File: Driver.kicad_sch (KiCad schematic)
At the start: 20 parts, among them Q1 NMOS, Q2 NMOS, Q3 NMOS, Q4 NMOS

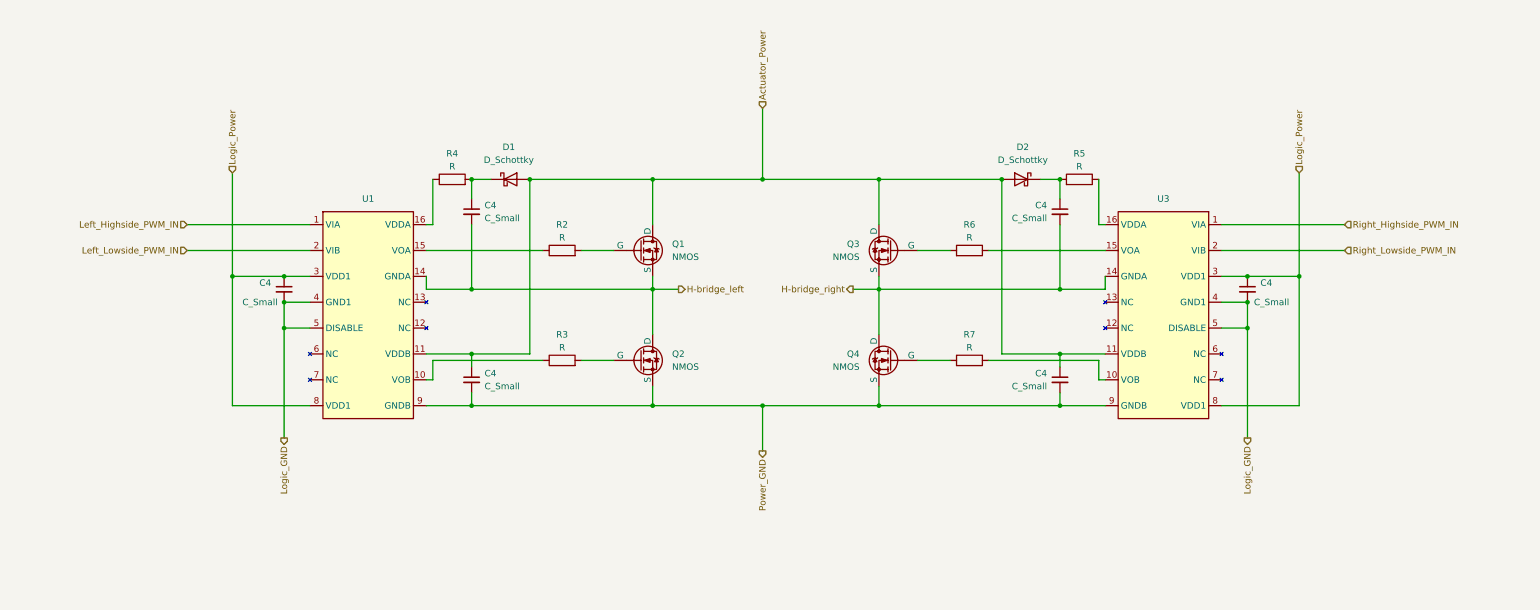
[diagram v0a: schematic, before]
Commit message: update Driver circuit
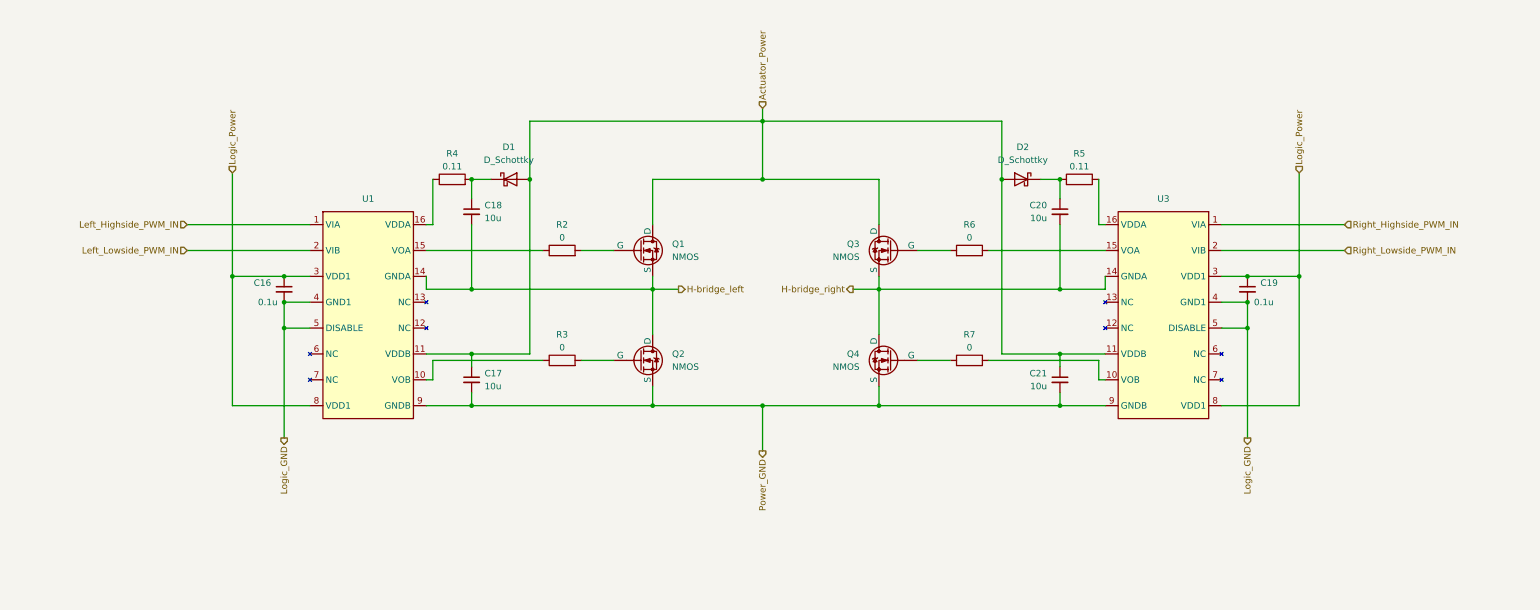
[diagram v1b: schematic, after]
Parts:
- C16, C19: renamed from C4; value C_Small -> 0.1u
- C17, C18, C20, C21: renamed from C4; value C_Small -> 10u
- R2, R3, R6, R7: value R -> 0
- R4, R5: value R -> 0.11
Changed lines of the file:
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@@
   (junction (at 127 106.68) (diameter 0) (color 0 0 0 0)
   )
+  (junction (at 54.61 109.22) (diameter 0) (color 0 0 0 0)
+  )
+  (junction (at 127 129.54) (diameter 0) (color 0 0 0 0)
+  )
+  (junction (at 148.59 73.66) (diameter 0) (color 0 0 0 0)
+  )
+  (junction (at 148.59 85.09) (diameter 0) (color 0 0 0 0)
+  )
+  (junction (at 243.84 104.14) (diameter 0) (color 0 0 0 0)
+  )
   (junction (at 195.58 85.09) (diameter 0) (color 0 0 0 0)
   )
-  (junction (at 54.61 109.22) (diameter 0) (color 0 0 0 0)
-  )
-  (junction (at 127 129.54) (diameter 0) (color 0 0 0 0)
-  )
-  (junction (at 171.45 85.09) (diameter 0) (color 0 0 0 0)
-  )
-  (junction (at 148.59 85.09) (diameter 0) (color 0 0 0 0)
-  )
-  (junction (at 243.84 104.14) (diameter 0) (color 0 0 0 0)
-  )
   (junction (at 243.84 114.3) (diameter 0) (color 0 0 0 0)
   )
@@
   (junction (at 44.45 104.14) (diameter 0) (color 0 0 0 0)
   )
+  (junction (at 102.87 85.09) (diameter 0) (color 0 0 0 0)
+  )
   (junction (at 207.01 129.54) (diameter 0) (color 0 0 0 0)
   )
@@
   (junction (at 243.84 109.22) (diameter 0) (color 0 0 0 0)
   )
-  (junction (at 102.87 85.09) (diameter 0) (color 0 0 0 0)
-  )
   (junction (at 91.44 85.09) (diameter 0) (color 0 0 0 0)
   )
@@
   (junction (at 91.44 129.54) (diameter 0) (color 0 0 0 0)
   )
-  (junction (at 127 85.09) (diameter 0) (color 0 0 0 0)
-  )
   (junction (at 91.44 119.38) (diameter 0) (color 0 0 0 0)
   )
@@
   (junction (at 148.59 129.54) (diameter 0) (color 0 0 0 0)
   )
+  (wire (pts (xy 102.87 85.09) (xy 102.87 73.66))
+    (stroke (width 0) (type default))
+  )
   (wire (pts (xy 214.63 124.46) (xy 215.9 124.46))
     (stroke (width 0) (type default))
@@
     (stroke (width 0) (type default))
   )
+  (wire (pts (xy 148.59 73.66) (xy 195.58 73.66))
+    (stroke (width 0) (type default))
+  )
   (wire (pts (xy 127 106.68) (xy 127 115.57))
     (stroke (width 0) (type default))
@@
     (stroke (width 0) (type default))
   )
-  (wire (pts (xy 148.59 71.12) (xy 148.59 85.09))
+  (wire (pts (xy 148.59 71.12) (xy 148.59 73.66))
     (stroke (width 0) (type default))
   )
@@
     (stroke (width 0) (type default))
   )
-  (wire (pts (xy 127 85.09) (xy 102.87 85.09))
-    (stroke (width 0) (type default))
-  )
   (wire (pts (xy 207.01 119.38) (xy 207.01 121.92))
     (stroke (width 0) (type default))
@@
     (stroke (width 0) (type default))
   )
+  (wire (pts (xy 102.87 73.66) (xy 148.59 73.66))
+    (stroke (width 0) (type default))
+  )
   (wire (pts (xy 262.89 93.98) (xy 238.76 93.98))
     (stroke (width 0) (type default))
@@
     (stroke (width 0) (type default))
   )
-  (wire (pts (xy 171.45 85.09) (xy 195.58 85.09))
-    (stroke (width 0) (type default))
-  )
   (wire (pts (xy 148.59 85.09) (xy 127 85.09))
     (stroke (width 0) (type default))
@@
     (stroke (width 0) (type default))
   )
+  (wire (pts (xy 148.59 73.66) (xy 148.59 85.09))
+    (stroke (width 0) (type default))
+  )
   (wire (pts (xy 148.59 129.54) (xy 127 129.54))
     (stroke (width 0) (type default))
@@
   )
   (wire (pts (xy 214.63 120.65) (xy 214.63 124.46))
+    (stroke (width 0) (type default))
+  )
+  (wire (pts (xy 195.58 73.66) (xy 195.58 85.09))
     (stroke (width 0) (type default))
   )
@@
       (effects (font (size 1.27 1.27)))
     )
-    (property "Value" "R" (at 109.22 96.52 90)
+    (property "Value" "0" (at 109.22 96.52 90)
       (effects (font (size 1.27 1.27)))
     )
@@
       (effects (font (size 1.27 1.27)))
     )
-    (property "Value" "R" (at 189.23 118.11 90)
+    (property "Value" "0" (at 189.23 118.11 90)
       (effects (font (size 1.27 1.27)))
     )
@@
   (symbol (lib_id "Device:C_Small") (at 207.01 124.46 0) (unit 1)
     (in_bom yes) (on_board yes) (dnp no)
-    (property "Reference" "C4" (at 204.47 123.1963 0)
-      (effects (font (size 1.27 1.27)) (justify right))
-    )
-    (property "Value" "C_Small" (at 204.47 125.73 0)
+    (property "Reference" "C21" (at 204.47 123.1963 0)
+      (effects (font (size 1.27 1.27)) (justify right))
+    )
+    (property "Value" "10u" (at 204.47 125.73 0)
       (effects (font (size 1.27 1.27)) (justify right))
     )
@@
     (instances
       (project "schematic_MD"
-        (path "/3152684b-d11f-4a9a-8e6c-09965044adbd"
-          (reference "C4") (unit 1)
-        )
         (path "/3152684b-d11f-4a9a-8e6c-09965044adbd/c42baef9-5835-4e28-8d2a-6c2cc5412fde"
           (reference "C21") (unit 1)
@@
       (effects (font (size 1.27 1.27)))
     )
-    (property "Value" "R" (at 109.22 118.11 90)
+    (property "Value" "0" (at 109.22 118.11 90)
       (effects (font (size 1.27 1.27)))
     )
@@
   (symbol (lib_id "Device:C_Small") (at 54.61 106.68 0) (unit 1)
     (in_bom yes) (on_board yes) (dnp no)
-    (property "Reference" "C4" (at 52.07 105.4163 0)
-      (effects (font (size 1.27 1.27)) (justify right))
-    )
-    (property "Value" "C_Small" (at 53.34 109.22 0)
+    (property "Reference" "C16" (at 52.07 105.4163 0)
+      (effects (font (size 1.27 1.27)) (justify right))
+    )
+    (property "Value" "0.1u" (at 53.34 109.22 0)
       (effects (font (size 1.27 1.27)) (justify right))
     )
@@
     (instances
       (project "schematic_MD"
-        (path "/3152684b-d11f-4a9a-8e6c-09965044adbd"
-          (reference "C4") (unit 1)
-        )
         (path "/3152684b-d11f-4a9a-8e6c-09965044adbd/c42baef9-5835-4e28-8d2a-6c2cc5412fde"
           (reference "C16") (unit 1)
@@
   (symbol (lib_id "Device:C_Small") (at 91.44 91.44 0) (mirror y) (unit 1)
     (in_bom yes) (on_board yes) (dnp no)
-    (property "Reference" "C4" (at 93.98 90.1763 0)
-      (effects (font (size 1.27 1.27)) (justify right))
-    )
-    (property "Value" "C_Small" (at 93.98 92.71 0)
+    (property "Reference" "C18" (at 93.98 90.1763 0)
+      (effects (font (size 1.27 1.27)) (justify right))
+    )
+    (property "Value" "10u" (at 93.98 92.71 0)
       (effects (font (size 1.27 1.27)) (justify right))
     )
@@
     (instances
       (project "schematic_MD"
-        (path "/3152684b-d11f-4a9a-8e6c-09965044adbd"
-          (reference "C4") (unit 1)
-        )
         (path "/3152684b-d11f-4a9a-8e6c-09965044adbd/c42baef9-5835-4e28-8d2a-6c2cc5412fde"
           (reference "C18") (unit 1)
@@
   (symbol (lib_id "Device:C_Small") (at 243.84 106.68 0) (mirror y) (unit 1)
     (in_bom yes) (on_board yes) (dnp no)
-    (property "Reference" "C4" (at 246.38 105.4163 0)
-      (effects (font (size 1.27 1.27)) (justify right))
-    )
-    (property "Value" "C_Small" (at 245.11 109.22 0)
+    (property "Reference" "C19" (at 246.38 105.4163 0)
+      (effects (font (size 1.27 1.27)) (justify right))
+    )
+    (property "Value" "0.1u" (at 245.11 109.22 0)
       (effects (font (size 1.27 1.27)) (justify right))
     )
@@
     (instances
       (project "schematic_MD"
-        (path "/3152684b-d11f-4a9a-8e6c-09965044adbd"
-          (reference "C4") (unit 1)
-        )
         (path "/3152684b-d11f-4a9a-8e6c-09965044adbd/c42baef9-5835-4e28-8d2a-6c2cc5412fde"
           (reference "C19") (unit 1)
@@
       (effects (font (size 1.27 1.27)))
     )
-    (property "Value" "R" (at 87.63 82.55 90)
+    (property "Value" "0.11" (at 87.63 82.55 90)
       (effects (font (size 1.27 1.27)))
     )
@@
       (effects (font (size 1.27 1.27)))
     )
-    (property "Value" "R" (at 210.82 82.55 90)
+    (property "Value" "0.11" (at 210.82 82.55 90)
       (effects (font (size 1.27 1.27)))
     )
@@
       (effects (font (size 1.27 1.27)))
     )
-    (property "Value" "R" (at 189.23 96.52 90)
+    (property "Value" "0" (at 189.23 96.52 90)
       (effects (font (size 1.27 1.27)))
     )
@@
   (symbol (lib_id "Device:C_Small") (at 207.01 91.44 0) (unit 1)
     (in_bom yes) (on_board yes) (dnp no)
-    (property "Reference" "C4" (at 204.47 90.1763 0)
-      (effects (font (size 1.27 1.27)) (justify right))
-    )
-    (property "Value" "C_Small" (at 204.47 92.71 0)
+    (property "Reference" "C20" (at 204.47 90.1763 0)
+      (effects (font (size 1.27 1.27)) (justify right))
+    )
+    (property "Value" "10u" (at 204.47 92.71 0)
       (effects (font (size 1.27 1.27)) (justify right))
     )
@@
     (instances
       (project "schematic_MD"
-        (path "/3152684b-d11f-4a9a-8e6c-09965044adbd"
-          (reference "C4") (unit 1)
-        )
         (path "/3152684b-d11f-4a9a-8e6c-09965044adbd/c42baef9-5835-4e28-8d2a-6c2cc5412fde"
           (reference "C20") (unit 1)
@@
   (symbol (lib_id "Device:C_Small") (at 91.44 124.46 0) (mirror y) (unit 1)
     (in_bom yes) (on_board yes) (dnp no)
-    (property "Reference" "C4" (at 93.98 123.1963 0)
-      (effects (font (size 1.27 1.27)) (justify right))
-    )
-    (property "Value" "C_Small" (at 93.98 125.73 0)
+    (property "Reference" "C17" (at 93.98 123.1963 0)
+      (effects (font (size 1.27 1.27)) (justify right))
+    )
+    (property "Value" "10u" (at 93.98 125.73 0)
       (effects (font (size 1.27 1.27)) (justify right))
     )
@@
     (instances
       (project "schematic_MD"
-        (path "/3152684b-d11f-4a9a-8e6c-09965044adbd"
-          (reference "C4") (unit 1)
-        )
         (path "/3152684b-d11f-4a9a-8e6c-09965044adbd/c42baef9-5835-4e28-8d2a-6c2cc5412fde"
           (reference "C17") (unit 1)

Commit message: update parts list
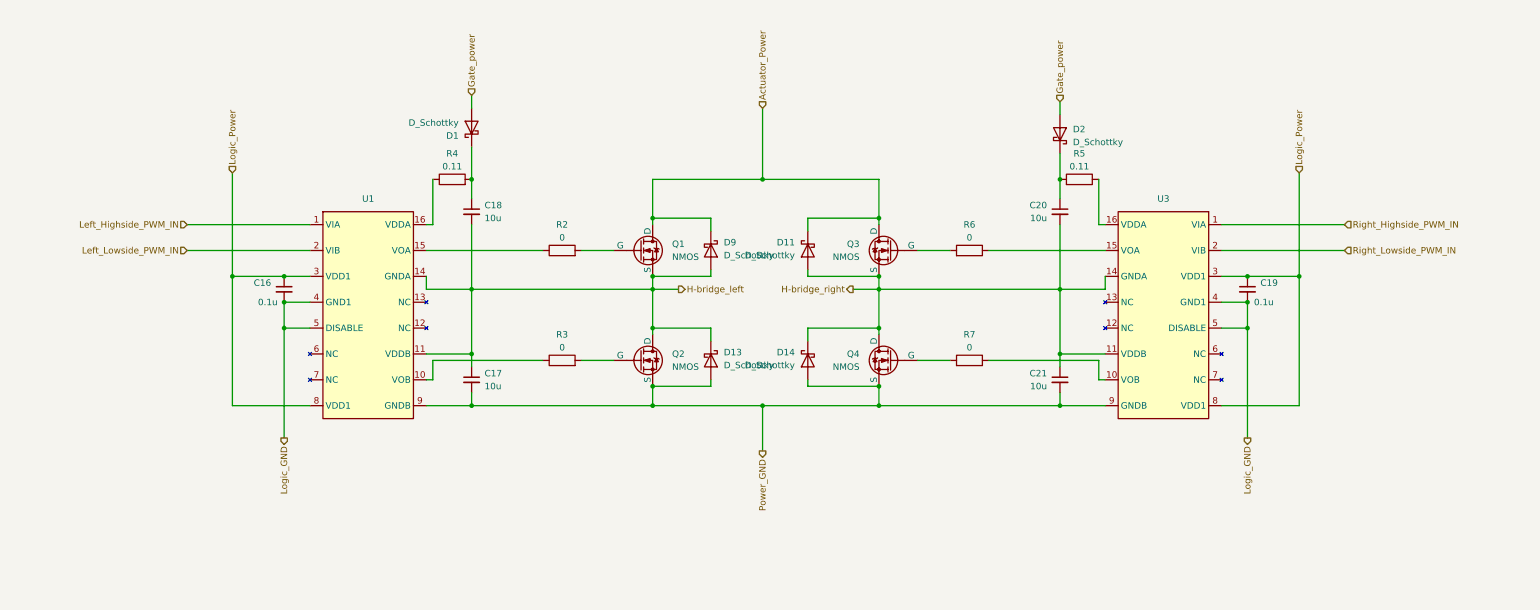
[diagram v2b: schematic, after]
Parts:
- added D11, D13, D14, D9: D_Schottky, symbol Device:D_Schottky
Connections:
- net Actuator_Power: now also D11.1 (K), D9.1 (K); no longer C17.1, C21.1, D1.2 (A), D2.2 (A), U1.11 (VDDB), U3.11 (VDDB)
- net H-bridge_left: now also C17.1, U1.11 (VDDB), D13.1 (K), D9.2 (A)
- net H-bridge_right: now also C21.1, U3.11 (VDDB), D11.2 (A), D14.1 (K)
- net Power_GND: now also D13.2 (A), D14.2 (A)
- new net Gate_power: D1.2 (A), D2.2 (A)

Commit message: Update motor driver circuit
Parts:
- removed Q1, Q2, Q3, Q4: NMOS, Package_TO_SOT_THT:TO-220-3_Horizontal_TabDown, symbol Simulation_SPICE:NMOS
- added Q1, Q3, Q5, Q7: SQJ886EP-T1_GE3, Package_SO:PowerPAK_SO-8L_Single, symbol RDC_generic:SQJ886EP-T1_GE3
- added U10: UCC21520ADW, Package_SO:SOIC-16W_7.5x10.3mm_P1.27mm, symbol Driver_FET:UCC21520ADW
- C16, C19: footprint (none) -> Capacitor_SMD:C_01005_0402Metric_Pad0.57x0.30mm_HandSolder
- C17, C18, C20, C21: footprint (none) -> Capacitor_SMD:C_1210_3225Metric_Pad1.33x2.70mm_HandSolder
- D1, D11, D13, D14, D2, D9: footprint (none) -> Diode_SMD:D_SOD-123F
- R2, R3, R6, R7: value 0 -> 10; footprint (none) -> Resistor_SMD:R_0805_2012Metric_Pad1.20x1.40mm_HandSolder
- R4, R5: value 0.11 -> 0.1; footprint (none) -> Resistor_SMD:R_1206_3216Metric_Pad1.30x1.75mm_HandSolder
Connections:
- net Actuator_Power: now also Q1.5 (D), Q5.5 (D)
- net H-bridge_left: now also Q1.1 (S), Q1.2 (S), Q1.3 (S), Q3.5 (D)
- net H-bridge_right: now also Q5.1 (S), Q5.2 (S), Q5.3 (S), Q7.5 (D)
- net Power_GND: now also Q3.1 (S), Q3.2 (S), Q3.3 (S), Q7.1 (S), Q7.2 (S), Q7.3 (S)
- net at R2.2: now also Q1.4 (G)
- net at R7.2: now also Q7.4 (G)
- net at R3.2: now also Q3.4 (G)
- net at R6.2: now also Q5.4 (G)
- new net: U10.3 (VCCI), U10.8 (VCCI)

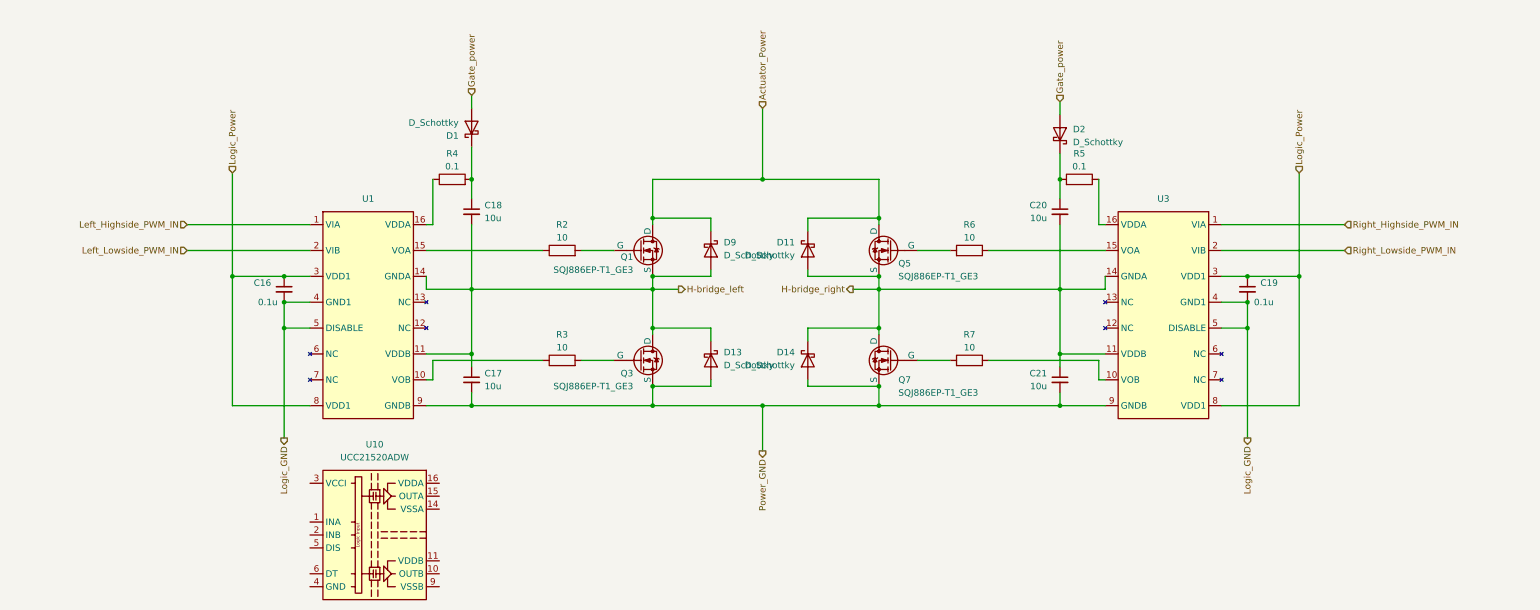
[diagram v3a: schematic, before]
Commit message: Change gate driver
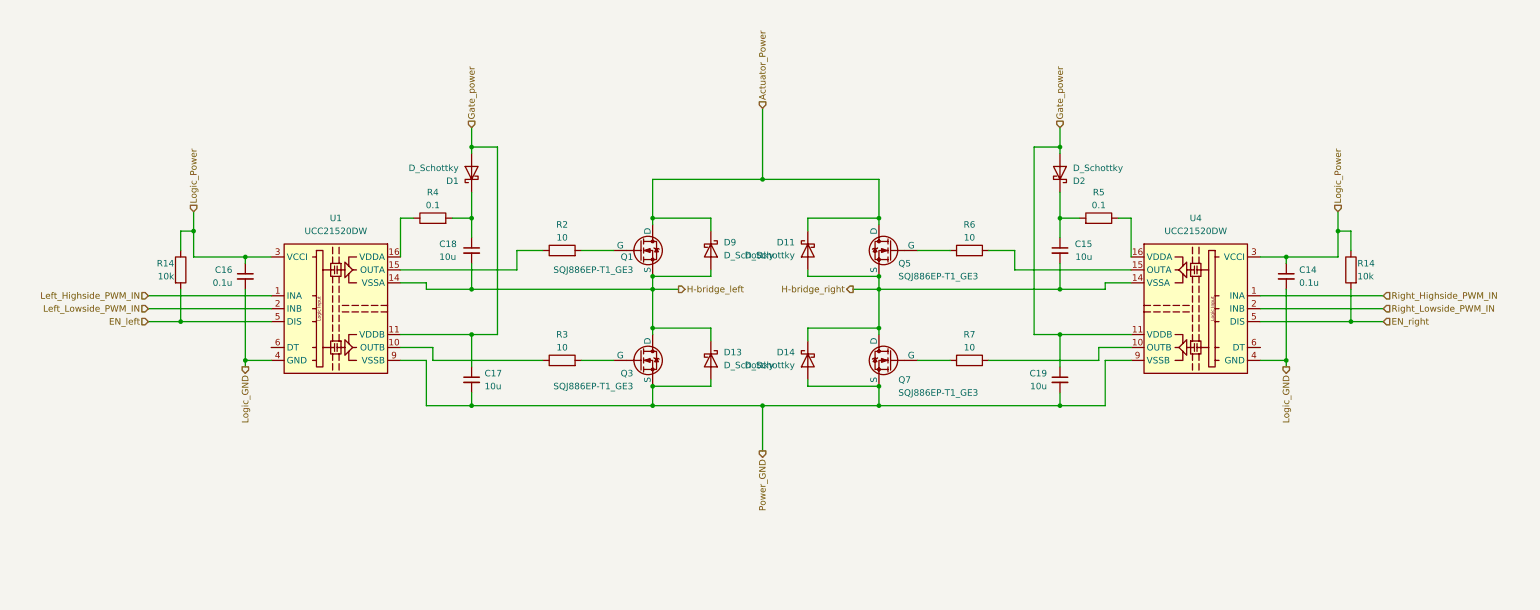
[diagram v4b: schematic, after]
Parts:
- removed C20, C21: 10u, Capacitor_SMD:C_1210_3225Metric_Pad1.33x2.70mm_HandSolder, symbol Device:C_Small
- removed U1, U3: ~, Package_SO:SOIC-16_3.9x9.9mm_P1.27mm, symbol RDC_generic:ADUM3223
- removed U10: UCC21520ADW, Package_SO:SOIC-16W_7.5x10.3mm_P1.27mm, symbol Driver_FET:UCC21520ADW
- added C14: 0.1u, Capacitor_SMD:C_01005_0402Metric_Pad0.57x0.30mm_HandSolder, symbol Device:C_Small
- added C15: 10u, Capacitor_SMD:C_1210_3225Metric_Pad1.33x2.70mm_HandSolder, symbol Device:C_Small
- added R14 (x2): 10k, Resistor_SMD:R_0402_1005Metric_Pad0.72x0.64mm_HandSolder, symbol Device:R
- added U1, U4: UCC21520DW, Package_SO:SOIC-16W_7.5x10.3mm_P1.27mm, symbol Driver_FET:UCC21520DW
- C19: value 0.1u -> 10u; footprint Capacitor_SMD:C_01005_0402Metric_Pad0.57x0.30mm_HandSolder -> Capacitor_SMD:C_1210_3225Metric_Pad1.33x2.70mm_HandSolder
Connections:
- net Gate_power: now also C17.1, C19.1, U1.11 (VDDB), U4.11 (VDDB)
- net H-bridge_left: now also U1.14 (VSSA); no longer C17.1
- net H-bridge_right: now also C15.2, U4.14 (VSSA)
- net Left_Highside_PWM_IN: now also U1.1 (INA)
- net Left_Lowside_PWM_IN: now also U1.2 (INB)
- net Logic_GND: now also C14.2, U1.4 (GND), U4.4 (GND); no longer C19.2
- net Logic_Power: now also C14.1, R14.1, R14.1, U1.3 (VCCI), U1.8 (VCCI), U4.3 (VCCI), U4.8 (VCCI); no longer C19.1
- net Power_GND: now also C19.2, U1.9 (VSSB), U4.9 (VSSB)
- net Right_Highside_PWM_IN: now also U4.1 (INA)
- net Right_Lowside_PWM_IN: now also U4.2 (INB)
- net at R2.1: now also U1.15 (OUTA)
- net at R7.1: now also U4.10 (OUTB)
- net at R6.1: now also U4.15 (OUTA)
- net at R5.1: now also U4.16 (VDDA)
- net at R3.1: now also U1.10 (OUTB)
- net at R4.1: now also U1.16 (VDDA)
- net at D2.1 (K), R5.2: now also C15.1
- new net EN_left: R14.2, U1.5 (DIS)
- new net EN_right: R14.2, U4.5 (DIS)
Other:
- moved on the sheet: C16, C18, D1, R4
